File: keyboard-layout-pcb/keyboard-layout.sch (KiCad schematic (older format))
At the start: 33 parts, among them J1 Conn_01x06, J2 Conn_01x02, J3 Conn_01x02, Q1 IRLB871, U1 TSOP384xx, U2 TSMP58000, U3 RFM9xLoRa

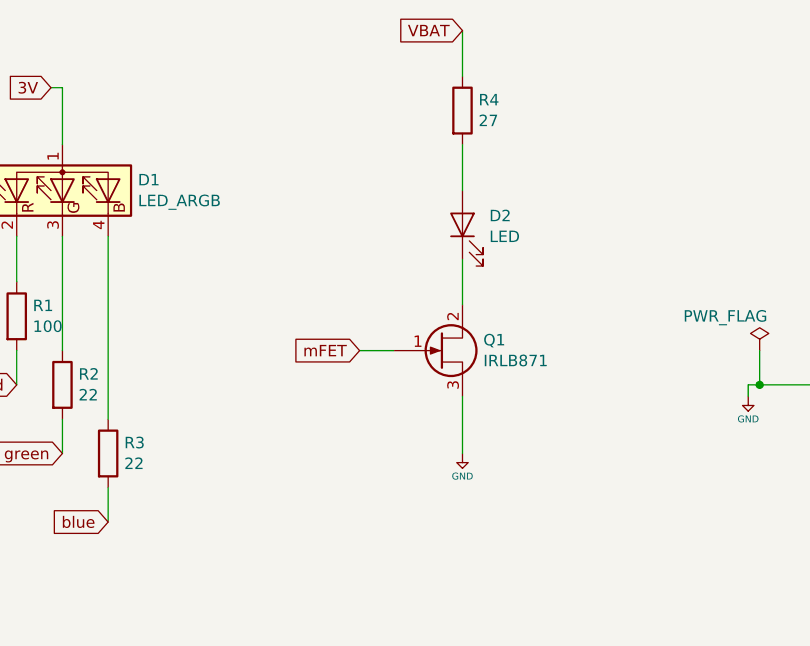
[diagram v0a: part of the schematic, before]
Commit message: Updated MOSFET footprint and netlist
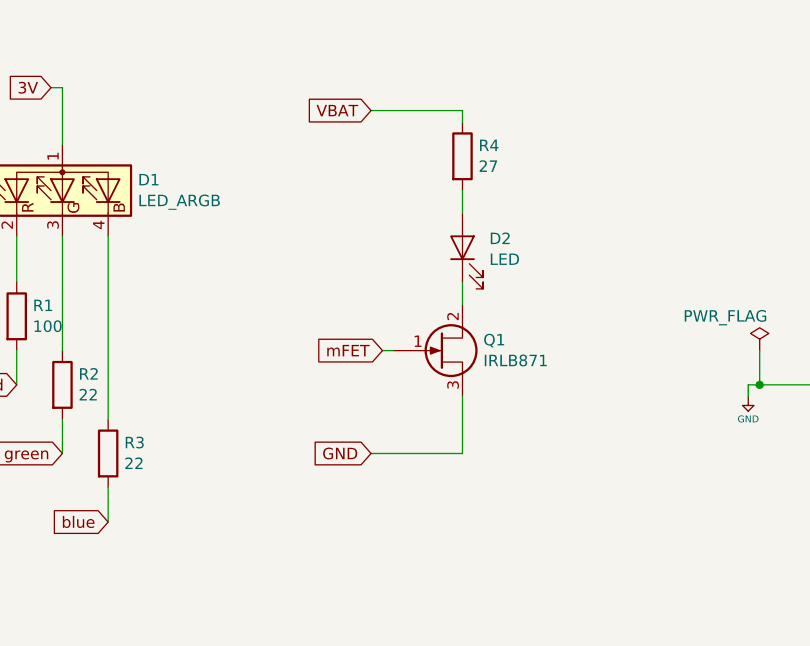
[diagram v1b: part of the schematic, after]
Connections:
- net +5V: no longer Q1.3 (S)
- new net GND: Q1.3 (S)
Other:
- moved on the sheet: D2, R4
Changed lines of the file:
@@
 L Device:R R4
 U 1 1 5DB26809
-P 6000 1650
-F 0 "R4" H 6070 1696 50  0000 L CNN
-F 1 "27" H 6070 1605 50  0000 L CNN
-F 2 "Resistors_THT:R_Axial_DIN0414_L11.9mm_D4.5mm_P15.24mm_Horizontal" V 5930 1650 50  0001 C CNN
-F 3 "~" H 6000 1650 50  0001 C CNN
-	1    6000 1650
+P 6000 1850
+F 0 "R4" H 6070 1896 50  0000 L CNN
+F 1 "27" H 6070 1805 50  0000 L CNN
+F 2 "Resistors_THT:R_Axial_DIN0414_L11.9mm_D4.5mm_P15.24mm_Horizontal" V 5930 1850 50  0001 C CNN
+F 3 "~" H 6000 1850 50  0001 C CNN
+	1    6000 1850
 	1    0    0    -1
 $EndComp
@@
 L Device:LED D2
 U 1 1 5DB2831D
-P 6000 2150
-F 0 "D2" V 6039 2033 50  0000 R CNN
-F 1 "LED" V 5948 2033 50  0000 R CNN
-F 2 "LEDs:LED_D5.0mm" H 6000 2150 50  0001 C CNN
-F 3 "~" H 6000 2150 50  0001 C CNN
-	1    6000 2150
+P 6000 2250
+F 0 "D2" V 6039 2133 50  0000 R CNN
+F 1 "LED" V 5948 2133 50  0000 R CNN
+F 2 "LEDs:LED_D5.0mm" H 6000 2250 50  0001 C CNN
+F 3 "~" H 6000 2250 50  0001 C CNN
+	1    6000 2250
 	0    -1   -1   0
 $EndComp
@@
 	1    0    0    -1
 $EndComp
-Wire Wire Line
-	6000 2300 6000 2500
-Wire Wire Line
-	6000 1800 6000 2000
 Text GLabel 9600 2550 2    50   Input ~ 0
 VBAT
 NoConn ~ 8100 2550
 NoConn ~ 8100 2750
-Text GLabel 6000 1300 0    50   Input ~ 0
+Text GLabel 5600 1650 0    50   Input ~ 0
 VBAT
-Wire Wire Line
-	6000 1300 6000 1500
 $Comp
 L Interface_Optical:TSOP384xx U1
@@
 Text GLabel 9600 3050 2    50   Output ~ 0
 mFET
-Text GLabel 5550 2700 0    50   Input ~ 0
+Text GLabel 5650 2700 0    50   Input ~ 0
 mFET
-Wire Wire Line
-	5550 2700 5700 2700
 Wire Wire Line
 	7950 3450 8100 3450
@@
 Wire Wire Line
 	5300 4700 5550 4700
-$Comp
-L keyboard_parts:GND #PWR0108
-U 1 1 5DC40DB6
-P 6000 3150
-F 0 "#PWR0108" H 6000 3200 20  0001 C CNN
-F 1 "GND" H 6000 3050 30  0000 C CNN
-F 2 "" H 6000 3150 60  0000 C CNN
-F 3 "" H 6000 3150 60  0000 C CNN
-	1    6000 3150
-	1    0    0    -1
-$EndComp
 Wire Wire Line
 	7250 2850 7250 2900
@@
 Wire Wire Line
 	5450 4300 5300 4300
+Text GLabel 5600 3150 0    50   Input ~ 0
+GND
+Wire Wire Line
+	5600 3150 6000 3150
+Wire Wire Line
+	5650 2700 5700 2700
+Wire Wire Line
+	5600 1650 6000 1650
+Wire Wire Line
+	6000 1650 6000 1700
+Wire Wire Line
+	6000 2000 6000 2100
+Wire Wire Line
+	6000 2400 6000 2500
 $EndSCHEMATC
